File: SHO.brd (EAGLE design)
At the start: 25.1 x 26 mm, 16 parts, among them Q1 BS170

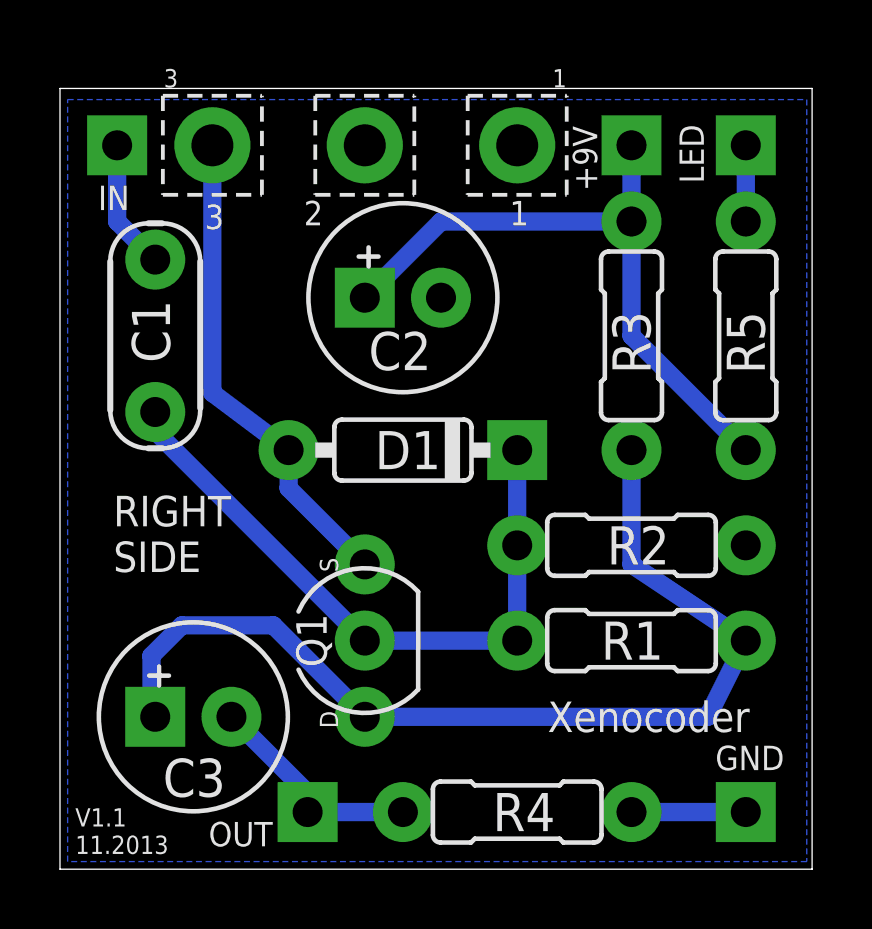
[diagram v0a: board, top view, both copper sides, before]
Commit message: Updated layout
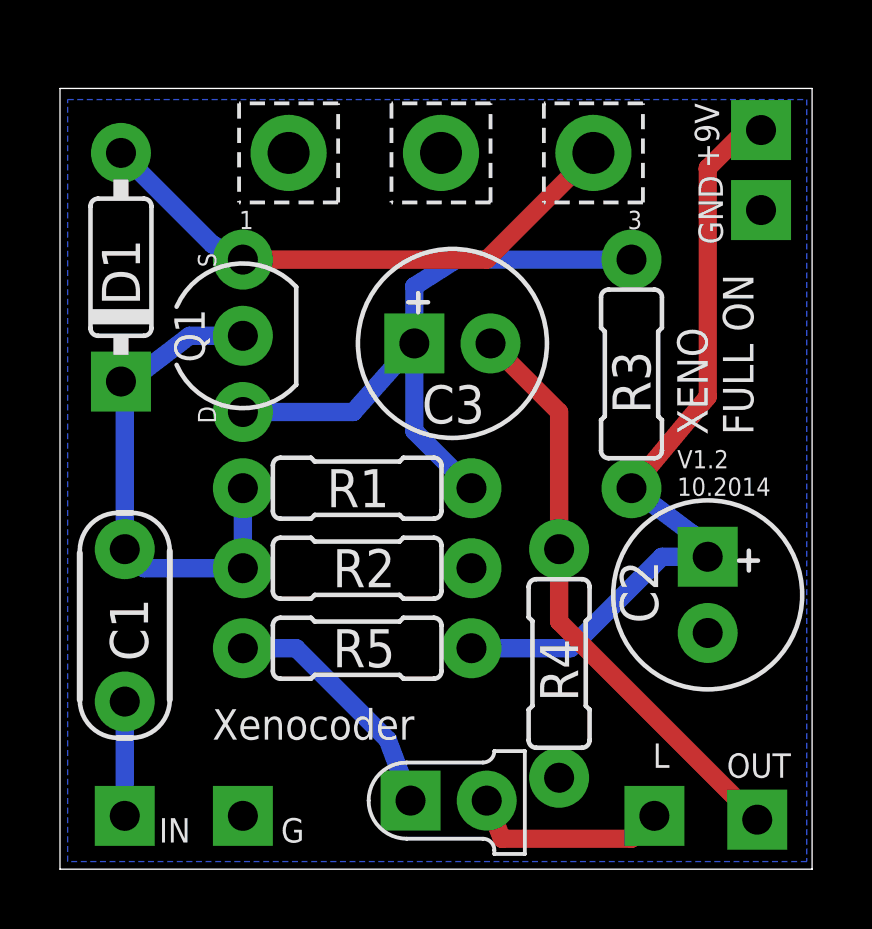
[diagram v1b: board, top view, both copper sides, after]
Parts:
- added G: GND(T), mb_supply:SQUARE
- added L: 3mm, mb_supply:SQUARE
- LED: value 3mm -> LED3MM; device mb_supply:SQUARE -> mb_diodes:LED3MM
- moved LED 24.0 mm to (13.0, 2.29)
- moved IN 22.4 mm to (2.16, 1.78)
- moved GND 20.1 mm to (23.4, 22.0)
- moved R5 16.6 mm to (9.91, 7.37), turned to 180 degrees
- moved C3 15.1 mm to (13.1, 17.5)
- moved OUT 15.0 mm to (23.2, 1.65)
- moved C2 14.2 mm to (21.6, 9.14), turned to 270 degrees
- moved D1 11.2 mm to (2.03, 20.1), turned to 90 degrees
- moved Q1 10.9 mm to (6.10, 17.8)
- moved R1 10.5 mm to (9.91, 12.7)
- moved C1 9.71 mm to (2.16, 8.13), turned to 90 degrees
- moved R2 9.18 mm to (9.91, 10.0)
- moved R4 5.15 mm to (16.6, 6.86), turned to 90 degrees
- moved +9V 4.35 mm to (23.4, 24.6)
- moved POT1 2.55 mm to (12.7, 23.9), turned to 180 degrees
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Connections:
- new net N$5: L.1, LED.K
- net GND: now also G.1
- net N$4: now also LED.A; no longer LED.1
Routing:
- net OUT: track 7.40 -> 19.6 mm
- net N$1: track 33.5 -> 21.8 mm
- net N$5: track 0.00 -> 6.76 mm
- net N$4: track 2.54 -> 8.26 mm
- net N$3: track 21.9 -> 17.0 mm
- net +9V: track 21.7 -> 26.3 mm
- net GND: track 3.81 -> 0.00 mm
- net N$2: track 16.3 -> 18.6 mm
- net IN: track 4.34 -> 3.81 mm
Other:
- board text added: "V1.2 10.2014"
- board text added: "XENO FULL ON"
- board text removed: "1"
- board text removed: "2"
- board text removed: "3"
- board text removed: "RIGHT SIDE"
- board text removed: "V1.1 11.2013"
